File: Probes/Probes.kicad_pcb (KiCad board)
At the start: 2 copper layers, 79.2 x 39 mm, 52 parts, among them IC1 ADUM1251ARZ, J1 Conn_Coaxial, J2 Conn_01x02_Male, J3 Conn_01x05_Male, J4 Conn_01x05_Male, J5 Conn_01x01_Female, J6 Conn_01x01_Female, J7 Conn_01x01_Female, J8 Conn_01x01_Female, U1 LMC6042IN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

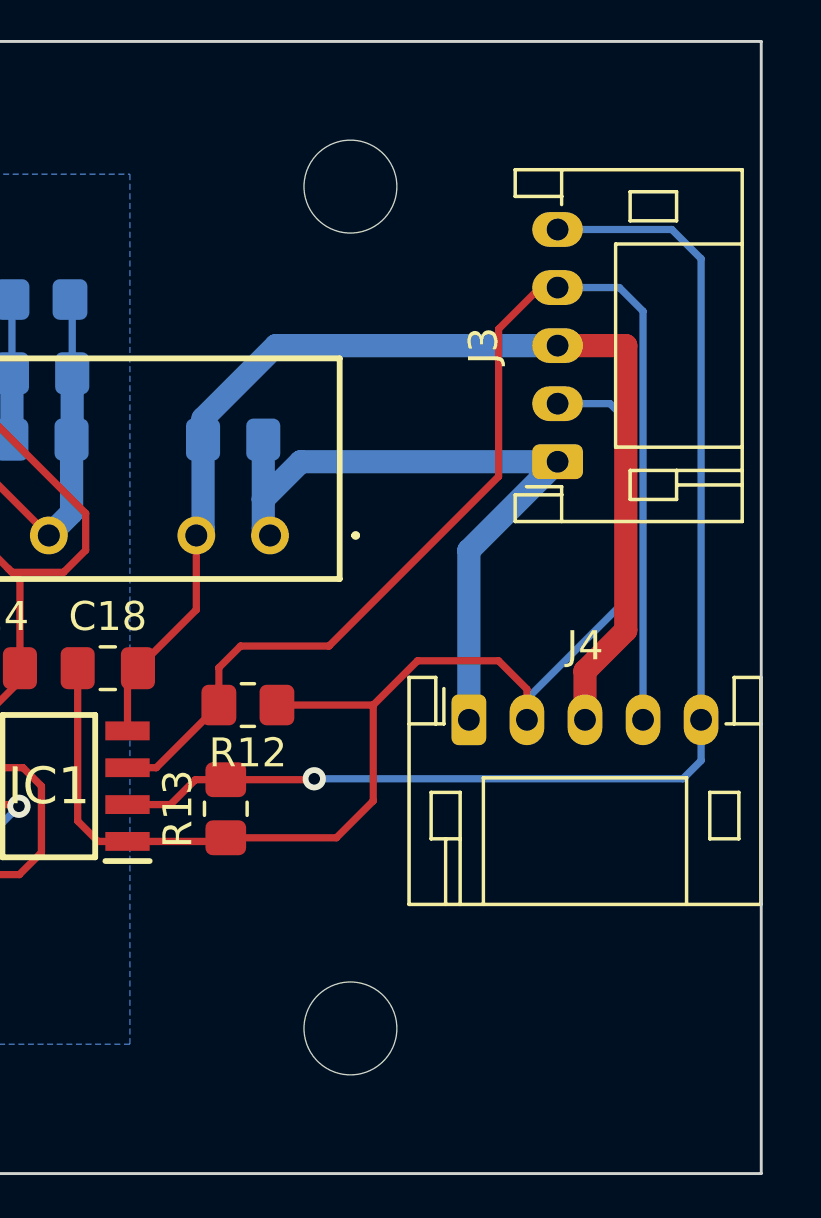
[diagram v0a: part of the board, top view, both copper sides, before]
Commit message: uneven copper distribution
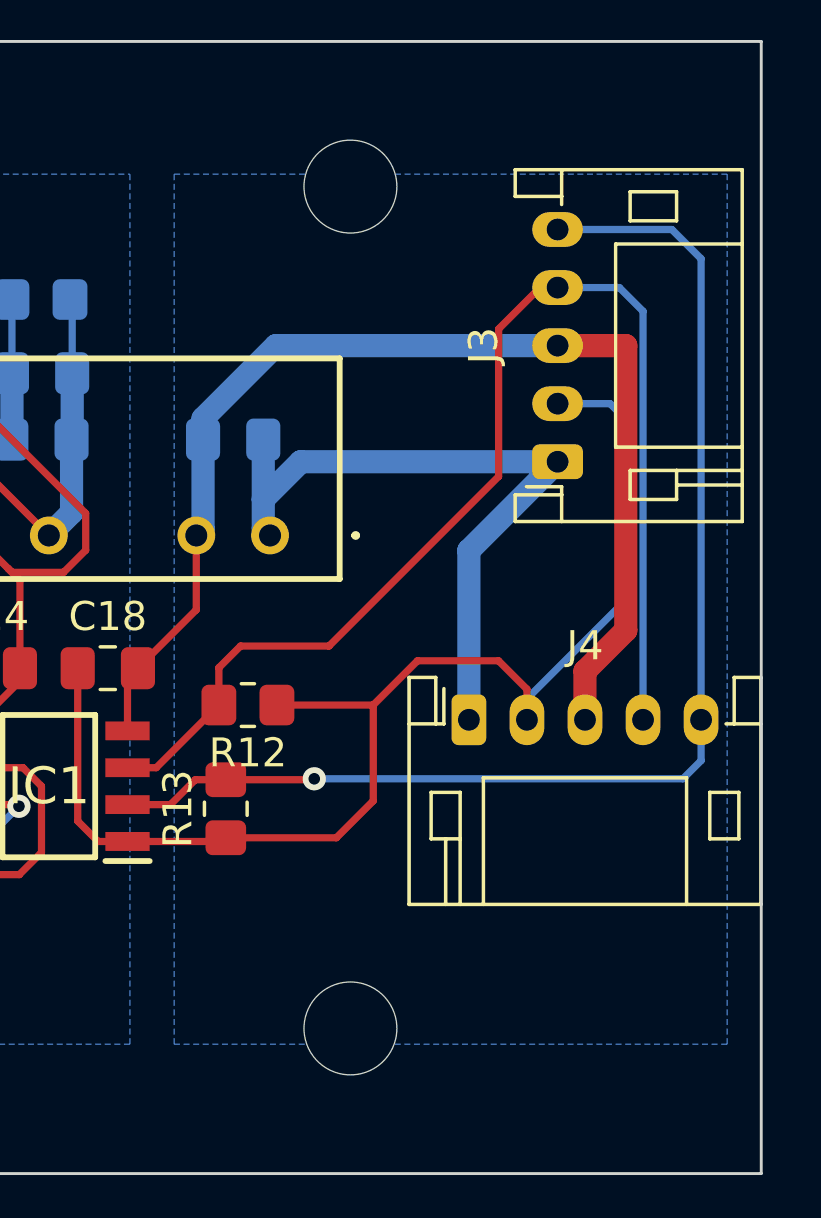
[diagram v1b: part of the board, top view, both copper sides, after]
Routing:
- added copper zone on B.Cu, net GNDPWR
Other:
- board text added: "3.3V"
- board text added: "5V"
- board text added: "GNDP"
- board text added: "SCL"
- board text added: "SDA"

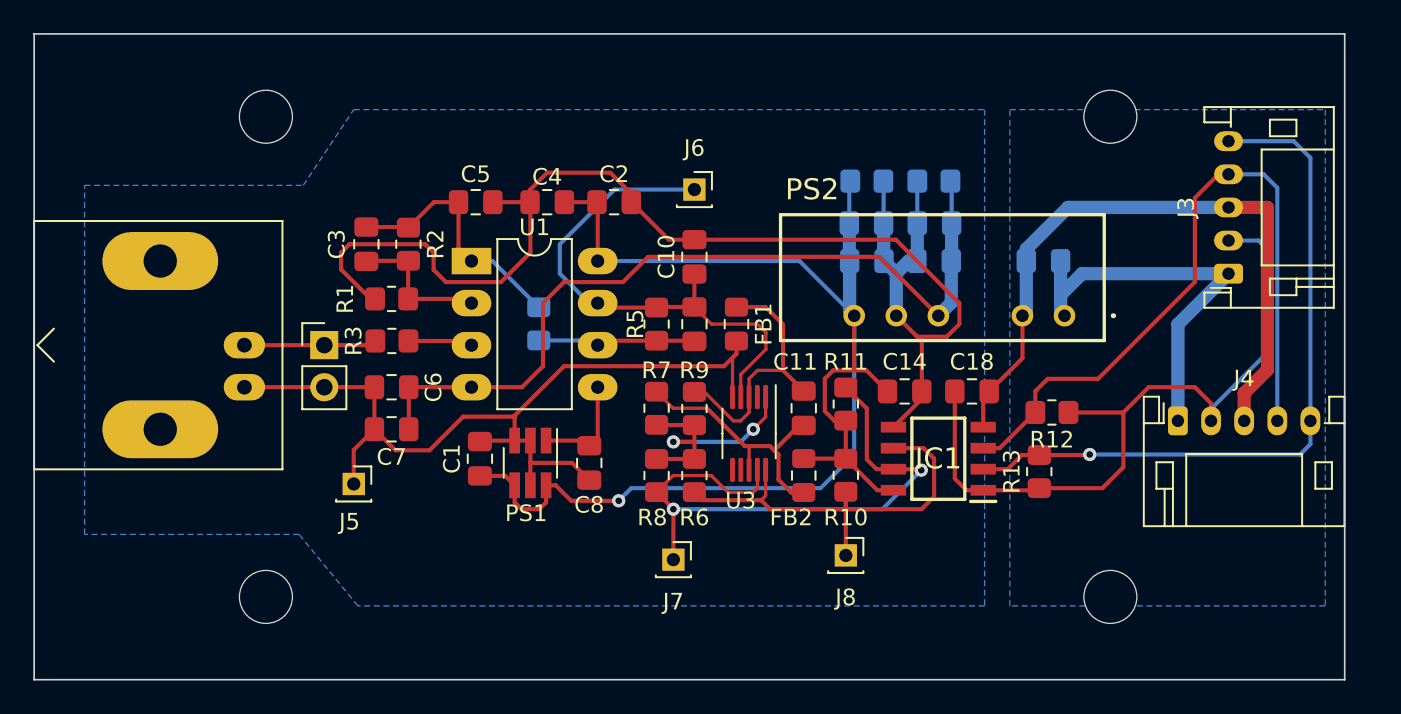
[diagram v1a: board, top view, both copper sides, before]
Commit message: move mounting holes
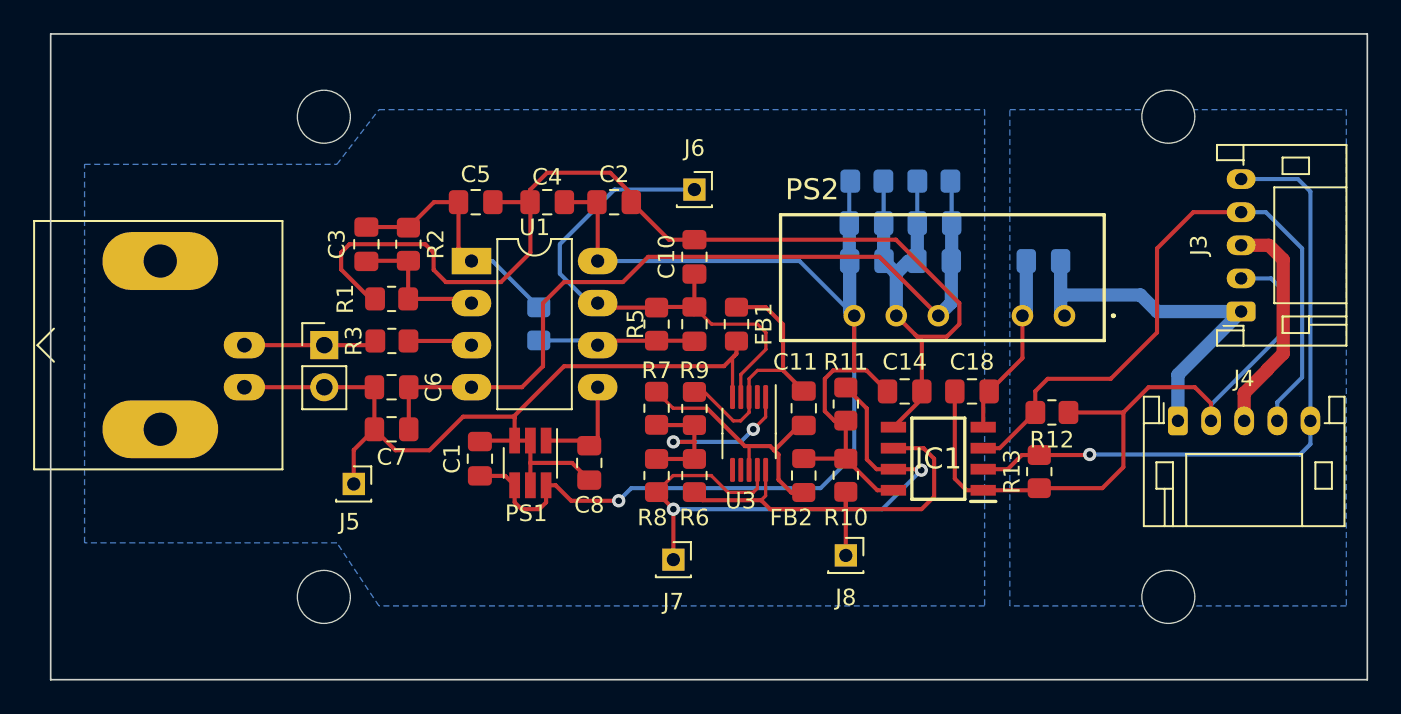
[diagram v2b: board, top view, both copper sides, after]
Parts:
- moved J3 2.41 mm to (137.2, 78.7)
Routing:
- net GNDPWR: track 40.9 -> 24.7 mm
- net SDA: track 43.2 -> 40.3 mm
- net SCL: track 42.8 -> 40.8 mm
- net +5VP: track 24.2 -> 22.9 mm
- net +3.3VP: track 45.1 -> 44.1 mm
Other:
- board size 79.2 x 39 mm -> 79.5 x 39 mm
